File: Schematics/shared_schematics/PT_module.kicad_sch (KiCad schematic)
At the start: 6 parts

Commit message: layout updates after review, cleaned up schematic organization
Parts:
- renumbered C5 to C28
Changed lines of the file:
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@@
 		)
 		(instances
-			(project ""
+			(project "upper_lc_board_v2"
 				(path "/8de962ac-ee95-4233-a205-efbcd04063bc/32a8ecec-3c56-4fc7-b1a3-95683e41c1c6/109a8a0a-c437-459f-9af6-d5e34f50799c"
 					(reference "#PWR0105")
@@
 				)
 			)
-			(project ""
+			(project "upper_lc_board_v2"
 				(path "/8de962ac-ee95-4233-a205-efbcd04063bc/32a8ecec-3c56-4fc7-b1a3-95683e41c1c6/109a8a0a-c437-459f-9af6-d5e34f50799c"
 					(reference "R13")
@@
 				)
 			)
-			(project ""
+			(project "upper_lc_board_v2"
 				(path "/8de962ac-ee95-4233-a205-efbcd04063bc/32a8ecec-3c56-4fc7-b1a3-95683e41c1c6/109a8a0a-c437-459f-9af6-d5e34f50799c"
 					(reference "J3")
@@
 				)
 			)
-			(project ""
+			(project "upper_lc_board_v2"
 				(path "/8de962ac-ee95-4233-a205-efbcd04063bc/32a8ecec-3c56-4fc7-b1a3-95683e41c1c6/109a8a0a-c437-459f-9af6-d5e34f50799c"
 					(reference "#PWR0107")
@@
 				)
 			)
-			(project ""
+			(project "upper_lc_board_v2"
 				(path "/8de962ac-ee95-4233-a205-efbcd04063bc/32a8ecec-3c56-4fc7-b1a3-95683e41c1c6/109a8a0a-c437-459f-9af6-d5e34f50799c"
 					(reference "R12")
@@
 				)
 			)
-			(project ""
+			(project "upper_lc_board_v2"
 				(path "/8de962ac-ee95-4233-a205-efbcd04063bc/32a8ecec-3c56-4fc7-b1a3-95683e41c1c6/109a8a0a-c437-459f-9af6-d5e34f50799c"
 					(reference "R11")
@@
 		)
 		(instances
-			(project ""
+			(project "upper_lc_board_v2"
 				(path "/8de962ac-ee95-4233-a205-efbcd04063bc/32a8ecec-3c56-4fc7-b1a3-95683e41c1c6/109a8a0a-c437-459f-9af6-d5e34f50799c"
 					(reference "#PWR0103")
@@
 				)
 			)
-			(project ""
+			(project "upper_lc_board_v2"
 				(path "/8de962ac-ee95-4233-a205-efbcd04063bc/32a8ecec-3c56-4fc7-b1a3-95683e41c1c6/109a8a0a-c437-459f-9af6-d5e34f50799c"
 					(reference "D11")
@@
 		(on_board yes)
 		(dnp no)
-		(property "Reference" "C5"
+		(property "Reference" "C28"
 			(at 175.006 89.154 0)
 			(effects
@@
 		)
 		(instances
-			(project ""
+			(project "upper_lc_board_v2"
 				(path "/8de962ac-ee95-4233-a205-efbcd04063bc/32a8ecec-3c56-4fc7-b1a3-95683e41c1c6/109a8a0a-c437-459f-9af6-d5e34f50799c"
 					(reference "C28")
@@
 		)
 		(instances
-			(project ""
+			(project "upper_lc_board_v2"
 				(path "/8de962ac-ee95-4233-a205-efbcd04063bc/32a8ecec-3c56-4fc7-b1a3-95683e41c1c6/109a8a0a-c437-459f-9af6-d5e34f50799c"
 					(reference "#PWR0104")

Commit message: swap I2C lines, add digi numbers to conns, fix diode issue
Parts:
- J?: Digikey 455-B02B-PASK-1-ND -> WM14965-ND
- R?: footprint Resistor_SMD:R_1206_3216Metric -> Resistor_SMD:R_0603_1608Metric; JLCPCB C4410 -> C21190
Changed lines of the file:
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@@
 			)
 		)
-		(property "Digikey" "455-B02B-PASK-1-ND"
+		(property "Digikey" "WM14965-ND"
 			(at 160.782 81.28 0)
 			(effects
@@
 			)
 		)
-		(property "Footprint" "Resistor_SMD:R_1206_3216Metric"
+		(property "Footprint" "Resistor_SMD:R_0603_1608Metric"
 			(at 146.812 84.582 90)
 			(effects
@@
 			)
 		)
-		(property "JLCPCB" "C4410"
+		(property "JLCPCB" "C21190"
 			(at 146.812 86.36 0)
 			(effects
@@
 		(fields_autoplaced yes)
 		(property "Reference" "D?"
+			(at 139.192 97.79 0)
+			(effects
+				(font
+					(size 1.27 1.27)
+				)
+			)
+		)
+		(property "Value" "BAV199DW"
 			(at 139.192 100.33 0)
-			(effects
-				(font
-					(size 1.27 1.27)
-				)
-			)
-		)
-		(property "Value" "BAV199DW"
-			(at 139.192 97.79 0)
 			(effects
 				(font
@@
 				)
 				(path "/8de962ac-ee95-4233-a205-efbcd04063bc/32a8ecec-3c56-4fc7-b1a3-95683e41c1c6/b149431a-f253-4ff6-90dc-e615cf93c3d3"
-					(reference "D12")
-					(unit 1)
-				)
-			)
+					(reference "D11")
+					(unit 2)
+				)
+			)

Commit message: resolve DRC & tweak
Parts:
- R?: value 60 -> 62
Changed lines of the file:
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@@
 			)
 		)
-		(property "Value" "60"
+		(property "Value" "62"
 			(at 153.162 82.55 90)
 			(effects

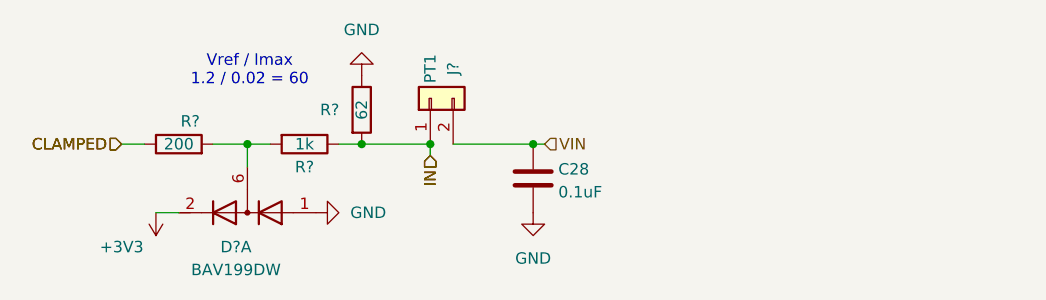
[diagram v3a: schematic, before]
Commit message: updated part numbers and fixed minor circuit issues
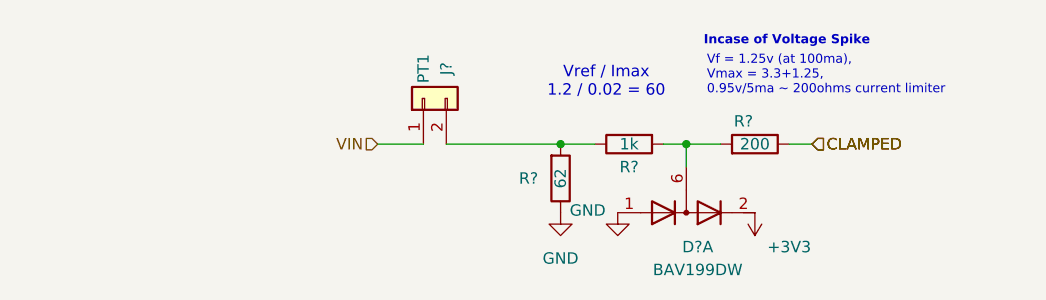
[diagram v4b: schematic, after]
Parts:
- removed C28: 0.1uF, Capacitor_SMD:C_0603_1608Metric, symbol Device:C
- D?: JLCPCB BAV199DW -> (none)
- R?: JLCPCB C8218 -> (none)
- R?: JLCPCB C21190 -> (none); LCSC C4410 -> C21190
- R?: Digikey 311-165CRCT-ND -> (none); LCSC (none) -> C23222
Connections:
- net VIN: now also J?.1 (Pin_1); no longer J?.2 (Pin_2)
- net IN: no longer names the net of R?.1, R?.2
- net IN: now also J?.2 (Pin_2); no longer J?.1 (Pin_1)
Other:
- note added: "Incase of Voltage Spike"
- note added: "Vf = 1.25v (at 100ma), Vmax = 3.3+1.25, 0.95v/5ma ~ 200ohms current limiter"
- moved on the sheet: D?A, J?, R?
